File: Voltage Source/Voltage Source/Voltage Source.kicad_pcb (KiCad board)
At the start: 2 copper layers, 95.9 x 22.2 mm, 40 parts, among them J1 PJ398SM, J2 PJ398SM, J3 Conn_01x01_Male, J4 Conn_01x01_Male, J5 Conn_02x05_Odd_Even, J6 Conn_02x05_Odd_Even, SW1 SW_DPDT_x2, SW2 SW_DPDT_x2, U1 TL072, U2 LM385BXZ-2.5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

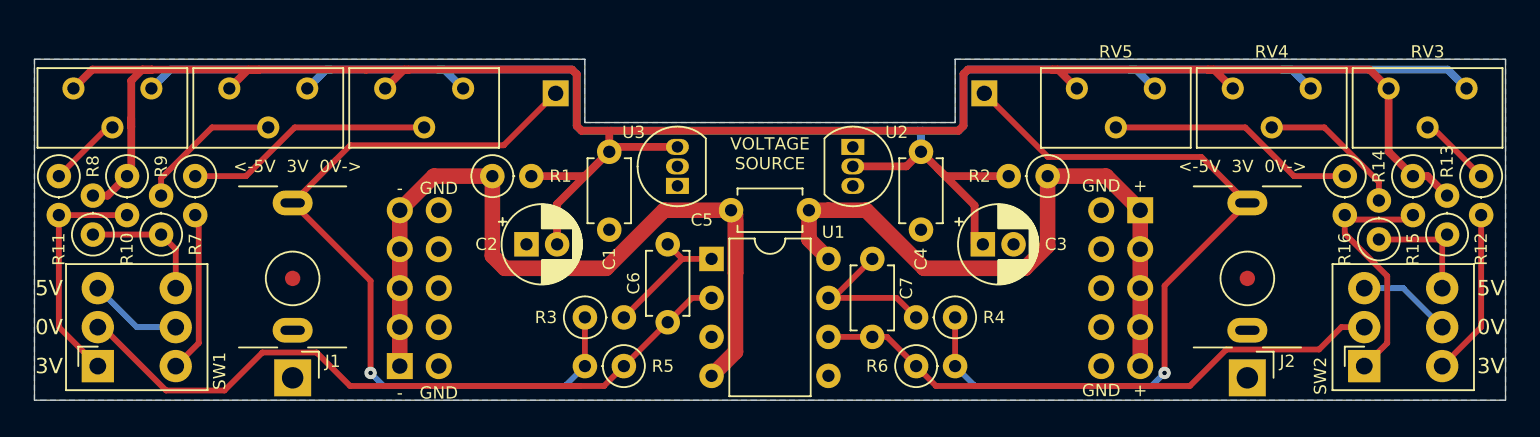
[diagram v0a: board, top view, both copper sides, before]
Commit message: Updated Voltage Source to REV 5
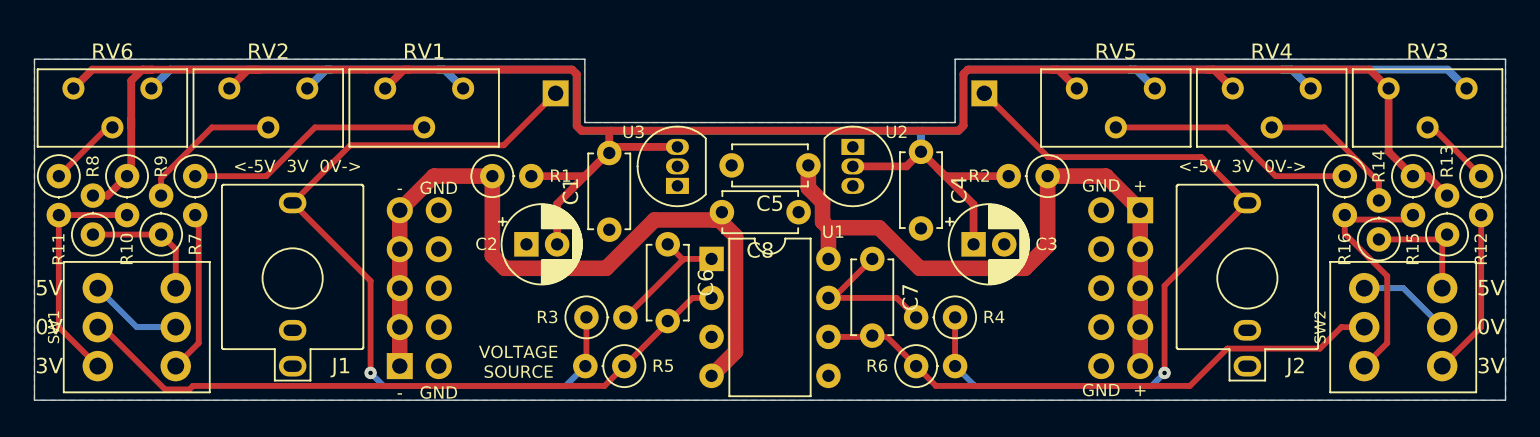
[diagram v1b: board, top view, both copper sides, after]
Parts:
- added C8: 100n, Capacitor_THT:C_Disc_D4.7mm_W2.5mm_P5.00mm, F.Cu at (1.86, -12.6)
- C1, C4, C6, C7: footprint NSI Footprints:C_Disc_D4mm_W2.6mm_P5.08mm -> Capacitor_THT:C_Disc_D4.7mm_W2.5mm_P5.00mm
- C2, C3: value 10u -> 2.2u
- C5: value 10n -> 100n; footprint NSI Footprints:C_Disc_D4mm_W2.6mm_P5.08mm -> Capacitor_THT:C_Disc_D4.7mm_W2.5mm_P5.00mm
- J1, J2: value PJ398SM -> WQP518MA; footprint NSI Footprints:Jack_3.5mm_QingPu_WQP-PJ398SM_Vertical_2HP -> Footprints:QingPu_WQP518MA
- R1, R2: value 3k -> 22k
- R10, R15: value 51k -> 12k
- R11, R16: value 750k -> 4.7M
- R13, R8: value 82k -> 20k
- R14, R9: value 1.3M -> 4.7M
- R5, R6: value 100k -> 24k
- RV1, RV2, RV3, RV4, RV5, RV6: footprint NSI Footprints:Potentiometer_TT_67Y_Vertical -> Potentiometer_THT:Potentiometer_Bourns_3296Y_Vertical
- SW1, SW2: footprint NSI Footprints:SW_Taiway_Sub_DPDT -> 2 Specific Footprints:SW_Sub_DPDT
- U1: value TL072 -> LF412
- moved C5 2.92 mm to (2.50, -15.6)
- moved C3 0.61 mm to (13.3, -10.5)
- moved R3 0.10 mm to (-12.0, -5.71)
- turned J1 to 90 degrees
- turned J2 to 90 degrees
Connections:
- C5 pad 2: VEE -> GND
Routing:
- net VEE: track 54.8 -> 50.8 mm
- net Net-(SW1A-B): track 46.9 -> 44.2 mm
- net VCC: track 43.1 -> 44.3 mm
- net Net-(J4-Pin_1): track 51.3 -> 51.9 mm
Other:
- rule pad_to_mask_clearance: 0.051 -> 0
- board text added: "VOLTAGE SOURCE REV 05"
- board text removed: "VOLTAGE SOURCE REV 04"

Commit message: changed current limiting resistors and 0V resistors, and cleaned up silk layer
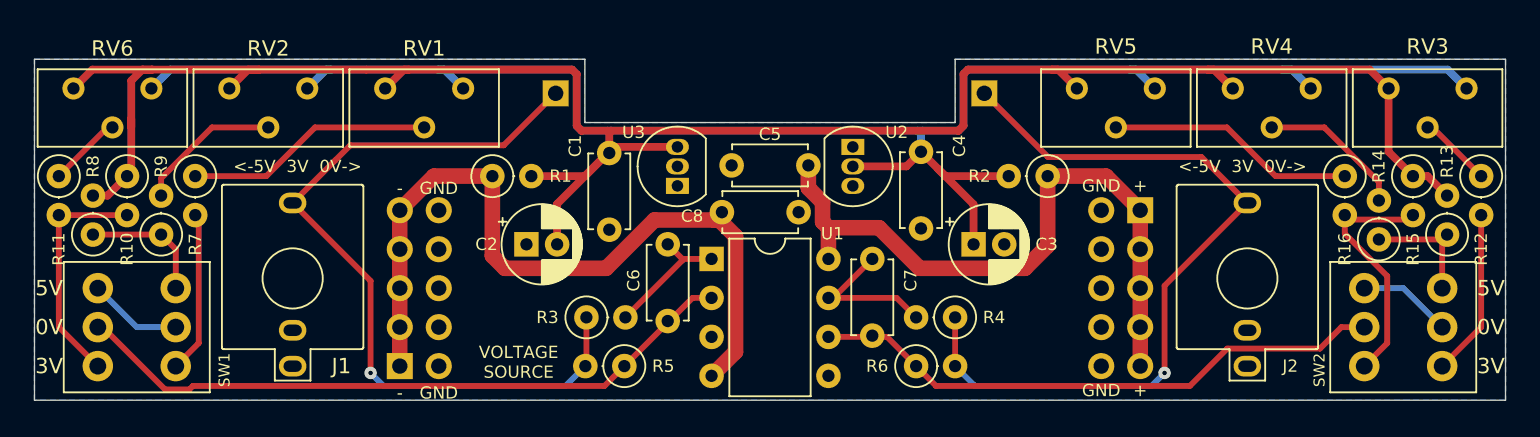
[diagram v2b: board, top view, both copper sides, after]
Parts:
- R1: value 22k -> 12k
- R11, R16: value 4.7M -> 750k
- R14, R9: value 4.7M -> 1.3M
- R2: value 22k -> 24k
